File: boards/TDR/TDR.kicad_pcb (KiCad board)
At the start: 4 copper layers, 60 x 37 mm, 128 parts, among them J1 USB_C_Receptacle_USB2.0, J2 SMA, U1 LFE5UM5G-45-CABGA381, U10 W25Q128JVPIQ, U11 93LCxxBxxOT, U12 FT2232HL, U13 MIC5504-3.3YM5, U14 Resistive_Power_Divider, U15 MCP4822, U2 USBLC6-2SC6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

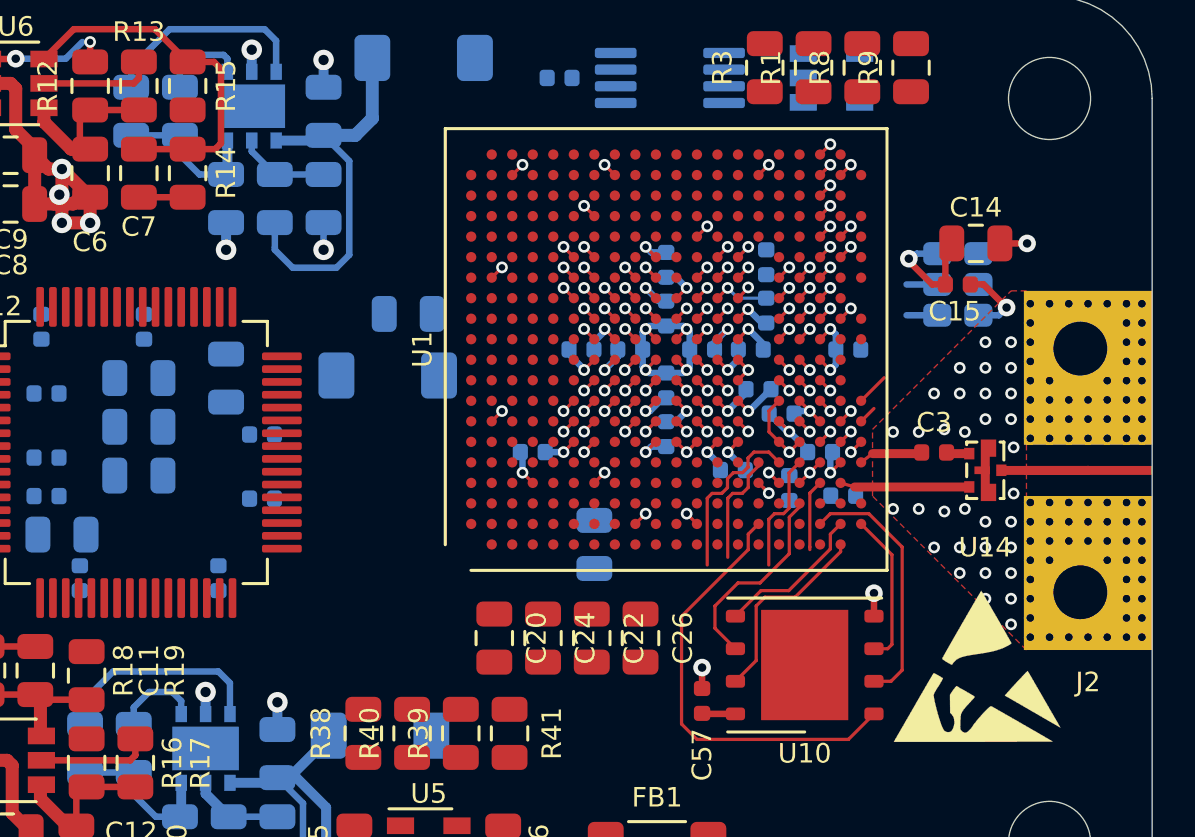
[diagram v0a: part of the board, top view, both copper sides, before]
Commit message: change crystal footprint and roughly finish schematic
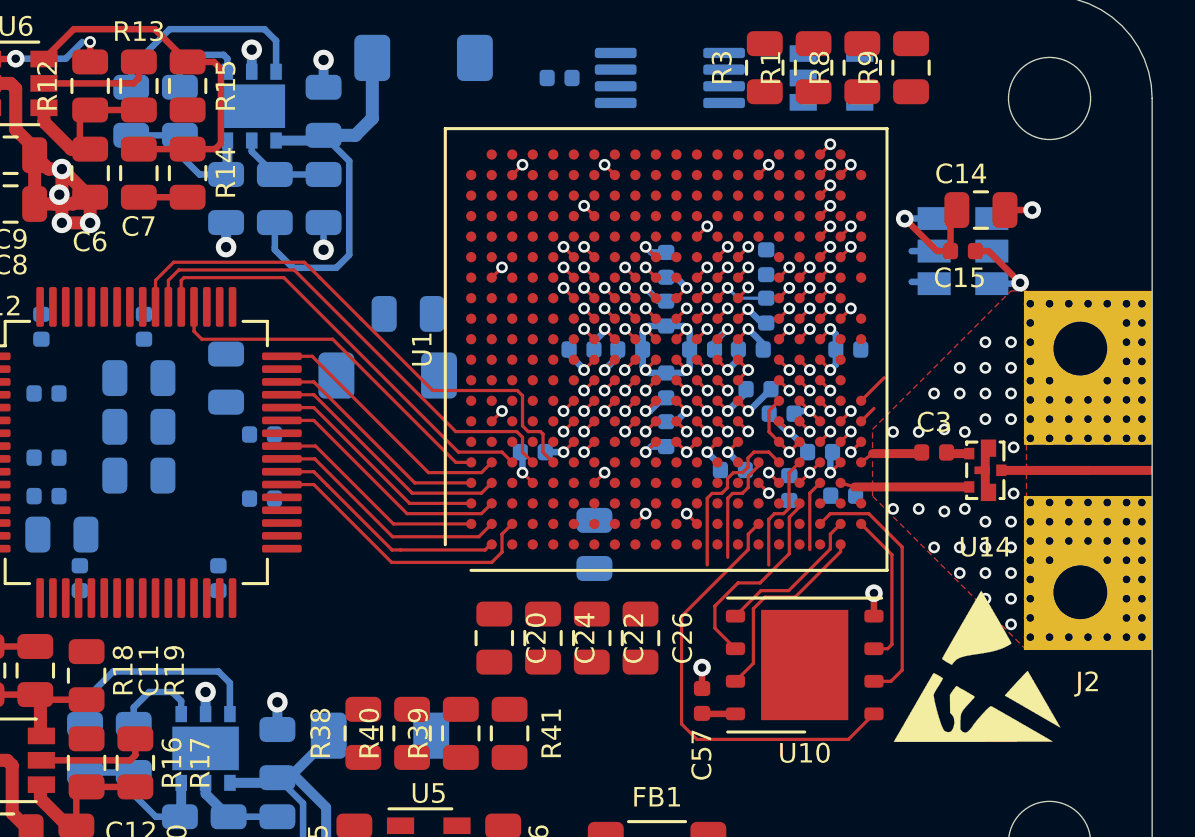
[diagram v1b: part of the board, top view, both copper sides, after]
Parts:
- U3: value AX3DBF1-200.0000 -> AxxDBF1-200.0000; footprint Moje:Oscillator_SMD_Abracon_LGA-6_2.5x3.2mm_P1.2mm -> Oscillator:Oscillator_SMD_IDT_JS6-6_5.0x3.2mm_P1.27mm
- moved C14 1.32 mm to (160.3, 71.3)
- moved C15 1.32 mm to (159.6, 73.0)
- moved U3 1.32 mm to (159.6, 73.0)
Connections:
- net /RX_D0CH1_N renamed /FPGA_IO/RX_D0CH1_N
- net /RX_D0CH1_P renamed /FPGA_IO/RX_D0CH1_P
- net /TX_D0CH1_N renamed /FPGA_IO/TX_D0CH1_N
- net /TX_D0CH1_P renamed /FPGA_IO/TX_D0CH1_P
- C20 pad 1: /FPGA_Power/VCCA -> /VCCA
- C22 pad 1: /FPGA_Power/VCCHTX -> +1V2_CORE
- C24 pad 1: /FPGA_Power/VCCA -> /VCCA
- C26 pad 1: /FPGA_Power/VCCHTX -> +1V2_CORE
- C28 pad 1: /FPGA_Power/VCCA -> /VCCA
- C30 pad 1: /FPGA_Power/VCCHTX -> +1V2_CORE
- C32 pad 1: /FPGA_Power/VCCA -> /VCCA
- C34 pad 1: /FPGA_Power/VCCHTX -> +1V2_CORE
- C36 pad 1: /FPGA_Power/VCCA -> /VCCA
- C38 pad 1: /FPGA_Power/VCCHTX -> +1V2_CORE
- FB1 pad 1: Net-(FB1-Pad1) -> /5V_INPUT
- FB2 pad 2: /FPGA_Power/VCCA -> /VCCA
- FB4 pad 2: /FPGA_Power/VCCHTX -> +1V2_CORE
- R1 pad 1: VCCA0 -> /VCCA
- R2 pad 2: VCCHTX0 -> +1V2_CORE
- U1 pad A2: Net-(U1-PadA2) -> /D3
- U1 pad A3: Net-(U1-PadA3) -> /D5
- U1 pad A4: Net-(U1-PadA4) -> /D7
- U1 pad A5: Net-(U1-PadA5) -> /TXE#
- U1 pad B1: Net-(U1-PadB1) -> /D1
- U1 pad B2: Net-(U1-PadB2) -> /D2
- U1 pad B3: Net-(U1-PadB3) -> /D4
- U1 pad B4: Net-(U1-PadB4) -> /D6
- U1 pad B5: Net-(U1-PadB5) -> /RXF#
- U1 pad C2: Net-(U1-PadC2) -> /D0
- U1 pad C5: Net-(U1-PadC5) -> /RD#
- U1 pad D5: Net-(U1-PadD5) -> /WR#
- U1 pad E5: Net-(U1-PadE5) -> /SIWU
- U1 pad H6: /FPGA_IO/VCCIO7 -> +3V3
- U1 pad H7: /FPGA_IO/VCCIO7 -> +3V3
- U1 pad J6: /FPGA_IO/VCCIO7 -> +3V3
- U1 pad T6: /FPGA_Power/VCCA -> /VCCA
- U1 pad T7: /FPGA_Power/VCCHTX -> +1V2_CORE
- U1 pad U6: /FPGA_Power/VCCA -> /VCCA
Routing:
- net /SIWU: track 0.00 -> 21.2 mm
- net /WR#: track 0.00 -> 18.9 mm
- net /RD#: track 0.00 -> 17.0 mm
- net /TXE#: track 0.00 -> 13.9 mm
- net /D0: track 0.00 -> 11.3 mm
- net /RXF#: track 0.00 -> 10.2 mm
- net /D6: track 0.00 -> 9.93 mm
- net /D4: track 0.00 -> 9.85 mm
- net /D2: track 0.00 -> 9.64 mm
- net /D1: track 0.00 -> 9.53 mm
- net /D7: track 0.00 -> 9.01 mm
- net /D5: track 0.00 -> 8.93 mm
- net /D3: track 0.00 -> 8.64 mm
- net VCCHTX0: track 2.74 -> 0.00 mm, vias 1 -> 0
- net +1V2_CORE: track 29.6 -> 32.3 mm, vias 20 -> 21
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
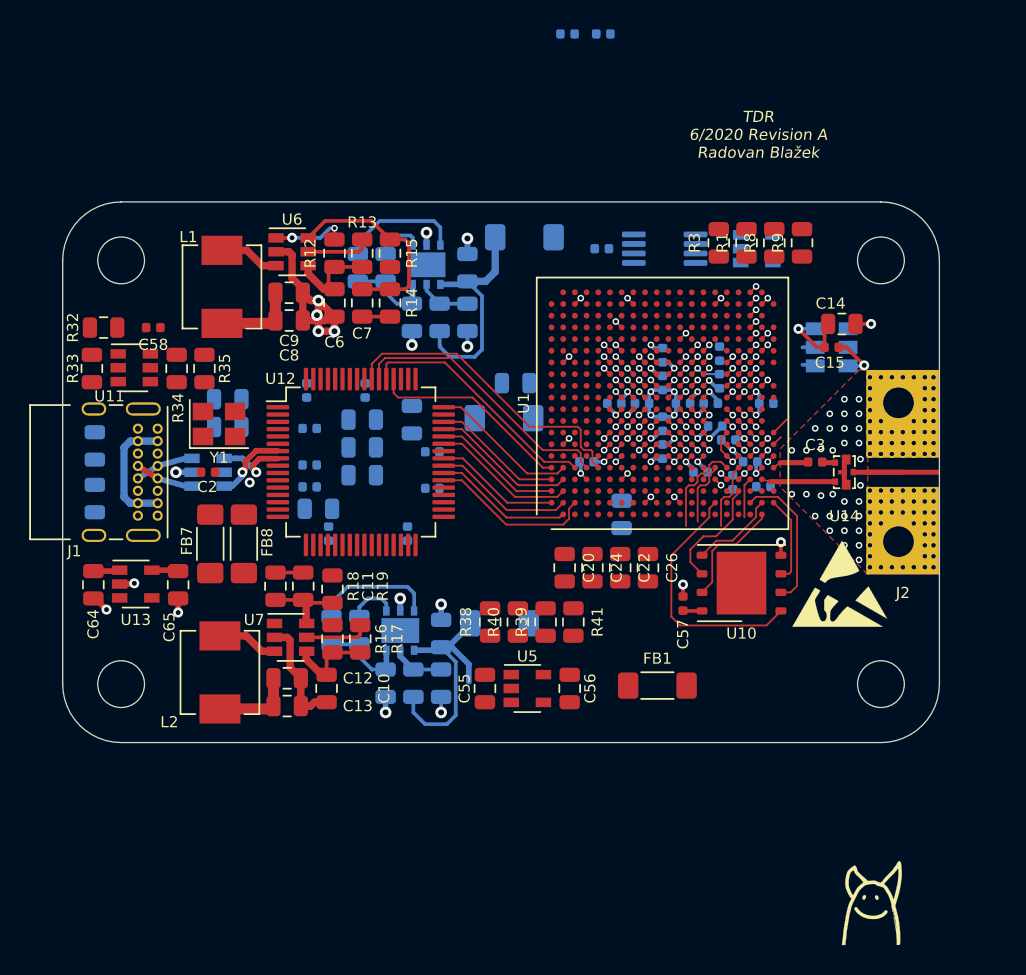
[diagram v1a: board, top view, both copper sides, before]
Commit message: change usb footprint, route a few connections
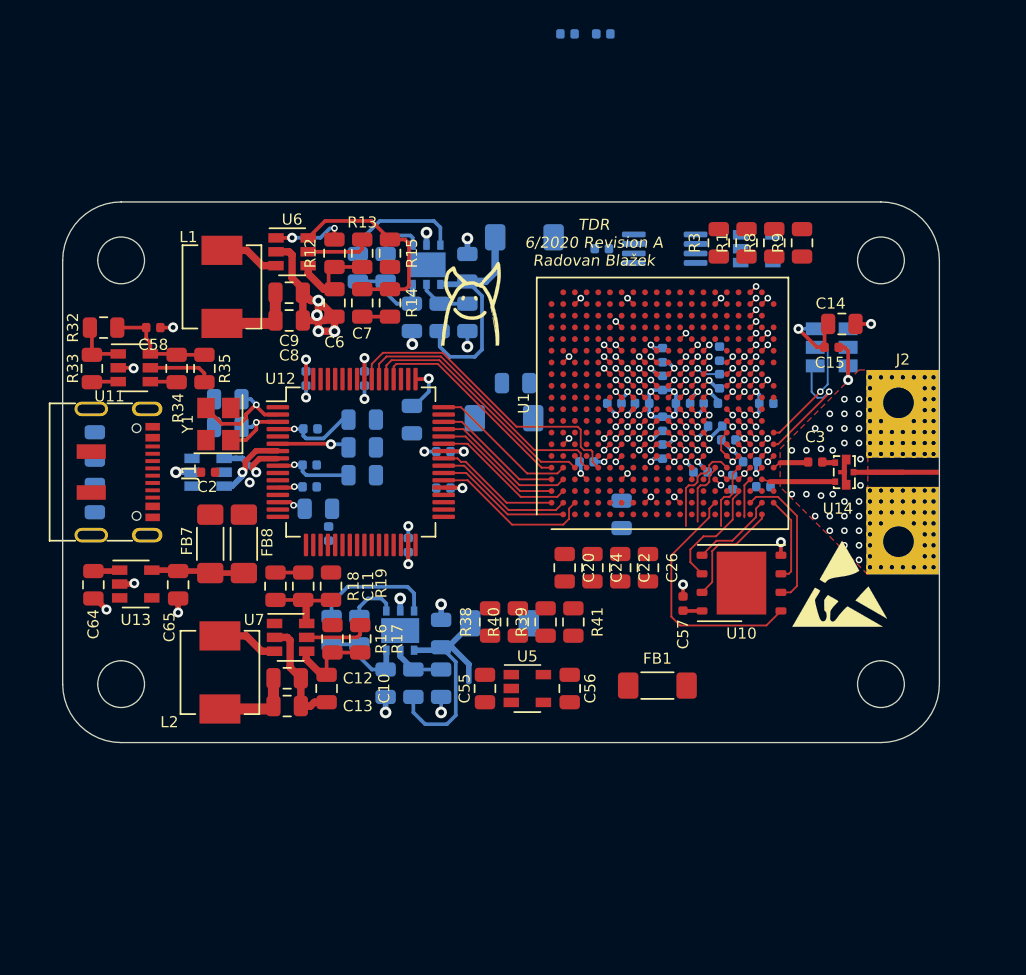
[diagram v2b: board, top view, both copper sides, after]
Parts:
- J1: footprint Connector_USB:USB_C_Receptacle_GCT_USB4085 -> Moje:USB_C_Receptacle_JAE_DX07S016
- moved G*** 49.4 mm to (135.0, 70.0)
- moved J1 5.43 mm to (109.0, 81.5)
- moved C68 0.82 mm to (123.7, 75.1)
- moved C71 0.82 mm to (127.7, 75.1)
- moved C70 0.79 mm to (130.7, 86.5)
- moved C67 0.76 mm to (133.1, 82.6)
- moved C73 0.76 mm to (133.1, 80.1)
- moved R19 0.22 mm to (125.4, 89.3)
- moved C60 0.06 mm to (124.0, 78.5)
- turned Y1 to 90 degrees
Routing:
- net /FT2232H/1.8V: track 0.00 -> 9.38 mm, vias 0 -> 4
- net /5V_INPUT: track 22.4 -> 14.0 mm
- net Net-(C58-Pad2): track 0.00 -> 7.62 mm
- net Net-(C61-Pad2): track 0.00 -> 7.57 mm, vias 0 -> 1
- net /REFCLK_D0_P: track 1.91 -> 8.78 mm, vias 0 -> 1
- net /FT2232H/VCCIO: track 0.00 -> 6.79 mm, vias 0 -> 3
- net GND: track 105.7 -> 111.7 mm, vias 139 -> 145
- net Net-(C59-Pad1): track 0.00 -> 5.93 mm, vias 0 -> 1
- net /REFCLK_D0_N: track 2.47 -> 8.38 mm, vias 0 -> 1
- net Net-(C1-Pad1): track 0.00 -> 5.42 mm, vias 0 -> 1
- net Net-(C62-Pad2): track 0.00 -> 5.18 mm, vias 0 -> 1
- net Net-(R36-Pad2): track 0.00 -> 4.94 mm, vias 0 -> 1
- net /FT2232H/3.3V_FTDI: track 1.83 -> 6.38 mm
- net Net-(R35-Pad2): track 0.00 -> 4.46 mm
- net /USB_D+: track 3.80 -> 0.00 mm
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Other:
- net class Default removed
- net class LVDS removed

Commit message: connect fpga vccio to 3.3V, add decoupling, route some tracks
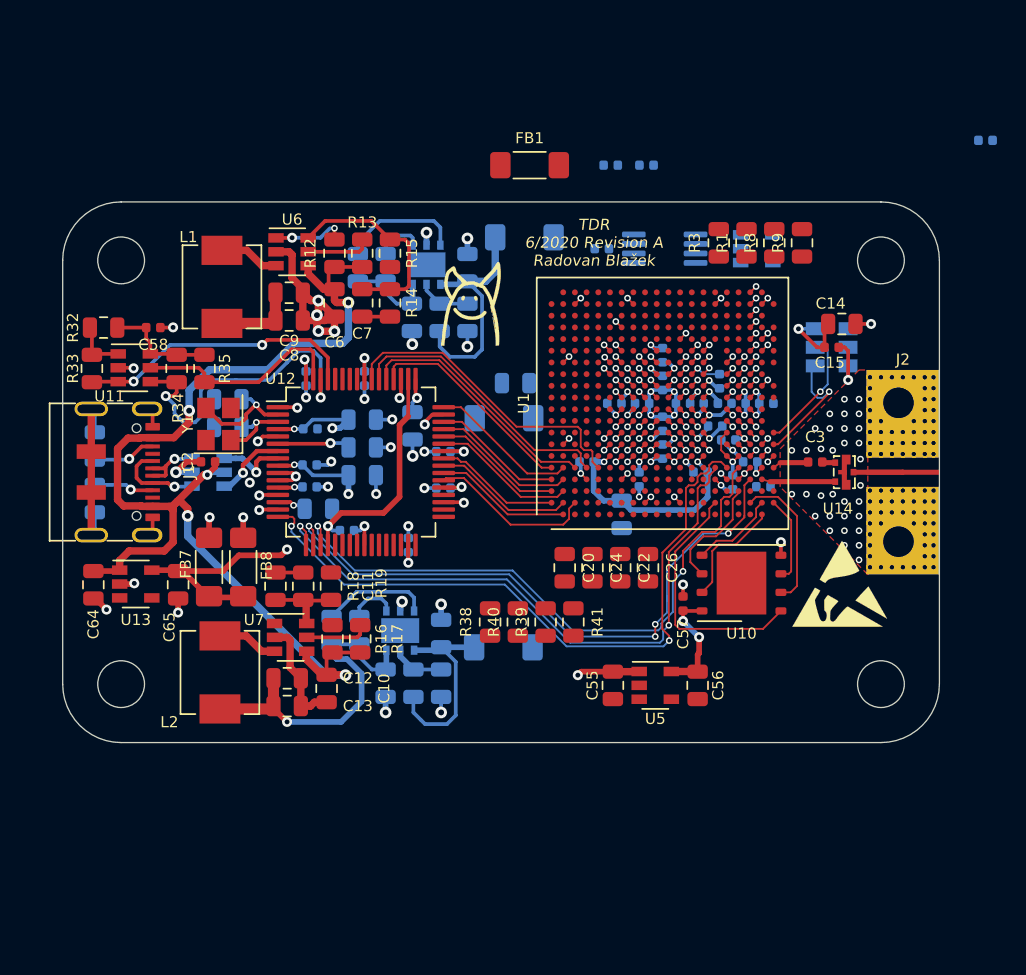
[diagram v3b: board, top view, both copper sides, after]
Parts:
- added C21: 100n, Capacitor_SMD:C_0402_1005Metric, B.Cu at (146.5, 82.0)
- added C5: 100n, Capacitor_SMD:C_0402_1005Metric, B.Cu at (153.3, 76.8)
- moved FB1 36.7 mm to (139.0, 60.5)
- moved C30 23.3 mm to (170.2, 58.8), turned to 0 degrees
- moved C32 9.46 mm to (147.0, 60.5)
- moved C36 9.46 mm to (144.5, 60.5)
- moved C56 8.76 mm to (150.5, 96.1)
- moved C55 8.76 mm to (144.7, 96.1)
- moved U5 8.76 mm to (147.6, 96.1)
- moved FB4 1.67 mm to (137.2, 93.5)
- moved FB7 1.59 mm to (117.0, 88.0)
- moved FB8 1.59 mm to (119.4, 88.0)
- moved C72 1.27 mm to (126.5, 85.5), turned to 0 degrees
- moved C2 0.72 mm to (117.0, 80.8)
- moved C66 0.43 mm to (130.9, 78.3)
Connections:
- C70 pad 1: /FT2232H/VCCIO -> /FT2232H/3.3V_FTDI
- C71 pad 1: /FT2232H/VCCIO -> /FT2232H/3.3V_FTDI
- C72 pad 1: /FT2232H/VCCIO -> /FT2232H/3.3V_FTDI
- C73 pad 1: /FT2232H/VCCIO -> /FT2232H/3.3V_FTDI
- R38 pad 1: /FT2232H/VCCIO -> /FT2232H/3.3V_FTDI
- R39 pad 1: /FT2232H/VCCIO -> /FT2232H/3.3V_FTDI
- R40 pad 1: /FT2232H/VCCIO -> /FT2232H/3.3V_FTDI
- U12 pad 20: /FT2232H/VCCIO -> /FT2232H/3.3V_FTDI
- U12 pad 31: /FT2232H/VCCIO -> /FT2232H/3.3V_FTDI
- U12 pad 42: /FT2232H/VCCIO -> /FT2232H/3.3V_FTDI
- U12 pad 56: /FT2232H/VCCIO -> /FT2232H/3.3V_FTDI
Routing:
- net /5V_INPUT: track 14.0 -> 98.4 mm, vias 0 -> 6
- net /FT2232H/3.3V_FTDI: track 6.38 -> 71.1 mm, vias 0 -> 5
- net GND: track 111.7 -> 153.4 mm, vias 145 -> 162
- net /TDO: track 2.77 -> 43.2 mm, vias 0 -> 4
- net /TCK: track 6.73 -> 46.9 mm, vias 0 -> 2
- net /TDI: track 4.42 -> 43.3 mm, vias 0 -> 2
- net /TMS: track 4.71 -> 42.1 mm, vias 0 -> 2
- net +3V3: track 3.01 -> 37.3 mm, vias 2 -> 7
- net /FT2232H/1.8V: track 9.38 -> 37.1 mm
- net Net-(R34-Pad2): track 1.82 -> 22.3 mm, vias 0 -> 2
- net Net-(R33-Pad2): track 1.82 -> 19.3 mm, vias 0 -> 2
- net Net-(C1-Pad1): track 5.42 -> 20.7 mm, vias 1 -> 3
- net Net-(C59-Pad1): track 5.93 -> 19.9 mm, vias 1 -> 3
- net +2V5: track 25.1 -> 37.4 mm, vias 1 -> 2
- net Net-(R35-Pad2): track 4.46 -> 14.8 mm
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
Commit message: route almost all nets except VCCA, VCCAUX and maybe some others
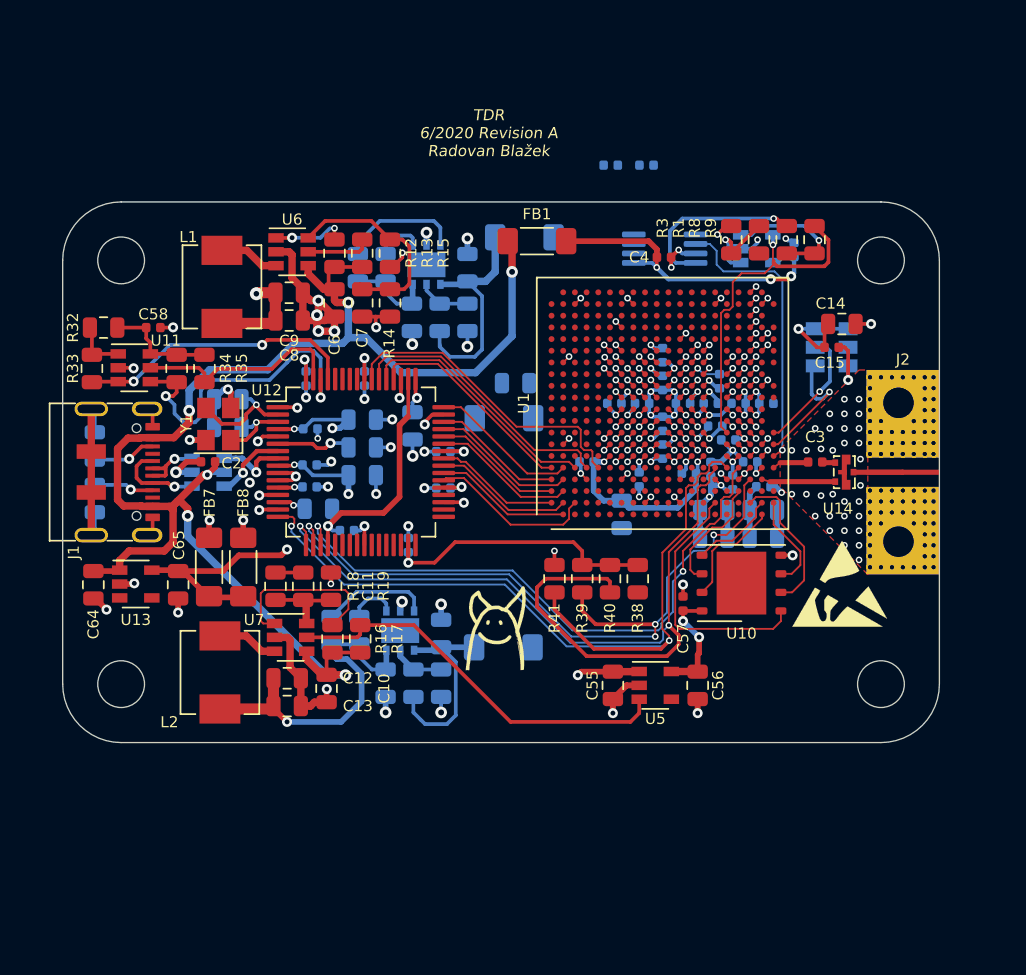
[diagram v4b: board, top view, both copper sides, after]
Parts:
- added C23: 100n, Capacitor_SMD:C_0402_1005Metric, B.Cu at (157.1, 66.3)
- C20, C22, C24, C26: moved to B.Cu
- C4: moved to F.Cu
- moved C30 29.3 mm to (151.4, 81.3), turned to -90 degrees
- moved G*** 22.3 mm to (136.7, 92.2)
- moved R38 10.5 mm to (146.4, 88.8), turned to -90 degrees
- moved C20 10.4 mm to (151.6, 86.0), turned to 180 degrees
- moved C22 10.0 mm to (155.0, 86.0), turned to 0 degrees
- moved C24 9.19 mm to (151.6, 84.1), turned to 180 degrees
- moved C26 8.83 mm to (155.0, 84.1), turned to 0 degrees
- moved R40 6.97 mm to (144.5, 88.8), turned to -90 degrees
- moved FB1 5.22 mm to (139.5, 65.7)
- moved C4 4.30 mm to (148.2, 66.8), turned to 0 degrees
- moved R39 3.88 mm to (142.6, 88.8), turned to -90 degrees
- moved R41 3.24 mm to (140.7, 88.8), turned to 90 degrees
- moved R8 0.88 mm to (156.6, 65.6)
- moved R9 0.88 mm to (158.5, 65.6)
- moved R1 0.88 mm to (154.7, 65.6)
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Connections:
- C22 pad 1: +1V2_CORE -> VCCHTX
- C26 pad 1: +1V2_CORE -> VCCHTX
- C30 pad 1: +1V2_CORE -> VCCHTX
- C34 pad 1: +1V2_CORE -> VCCHTX
- C38 pad 1: +1V2_CORE -> VCCHTX
- FB4 pad 2: +1V2_CORE -> VCCHTX
- R2 pad 2: +1V2_CORE -> VCCHTX
- U1 pad T7: +1V2_CORE -> VCCHTX
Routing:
- net GND: track 153.4 -> 184.6 mm, vias 162 -> 178
- net +1V2_CORE: track 32.3 -> 62.8 mm, vias 21 -> 22
- net /OUT_A: track 0.00 -> 23.3 mm, vias 0 -> 1
- net /FPGA_Power/2.5V_PG: track 4.42 -> 27.5 mm
- net Net-(C23-Pad1): track 0.00 -> 22.0 mm, vias 0 -> 3
- net /TDI: track 43.3 -> 63.7 mm
- net /5V_INPUT: track 98.4 -> 118.3 mm, vias 6 -> 7
- net /OUT_B: track 0.57 -> 19.9 mm
- net /FT2232H/3.3V_FTDI: track 71.1 -> 88.6 mm
- net Net-(R8-Pad2): track 0.00 -> 12.3 mm, vias 0 -> 1
- net Net-(R16-Pad2): track 0.00 -> 11.7 mm
- net /TCK: track 46.9 -> 57.2 mm
- net Net-(R8-Pad1): track 0.00 -> 8.94 mm, vias 0 -> 1
- net VCCHTX: track 0.00 -> 8.26 mm, vias 0 -> 1
- net /TDO: track 43.2 -> 49.8 mm
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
